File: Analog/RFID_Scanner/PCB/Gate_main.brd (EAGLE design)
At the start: 160 x 100 mm, 14 parts

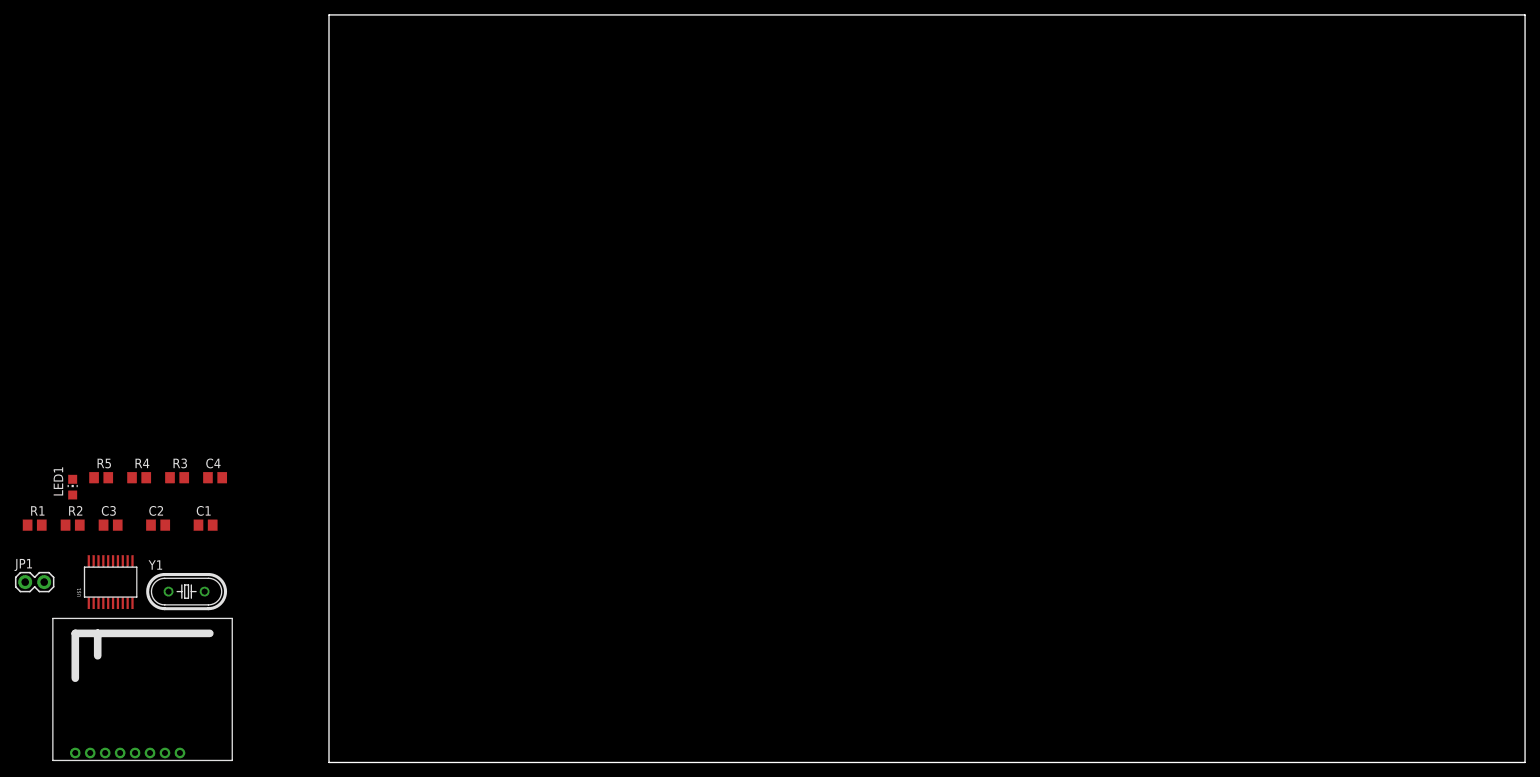
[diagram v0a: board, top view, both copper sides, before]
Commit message: PCB and firmware
Gate PCB 70% completed, need to figure out pinout for MCU and layout
signal amps.  Board size reduced by 50%.  Also need to add testpoints
Robot PCB PSU layout completed, motor and stepper drivers will move to
separate PCB
Created firmware files, w/o code
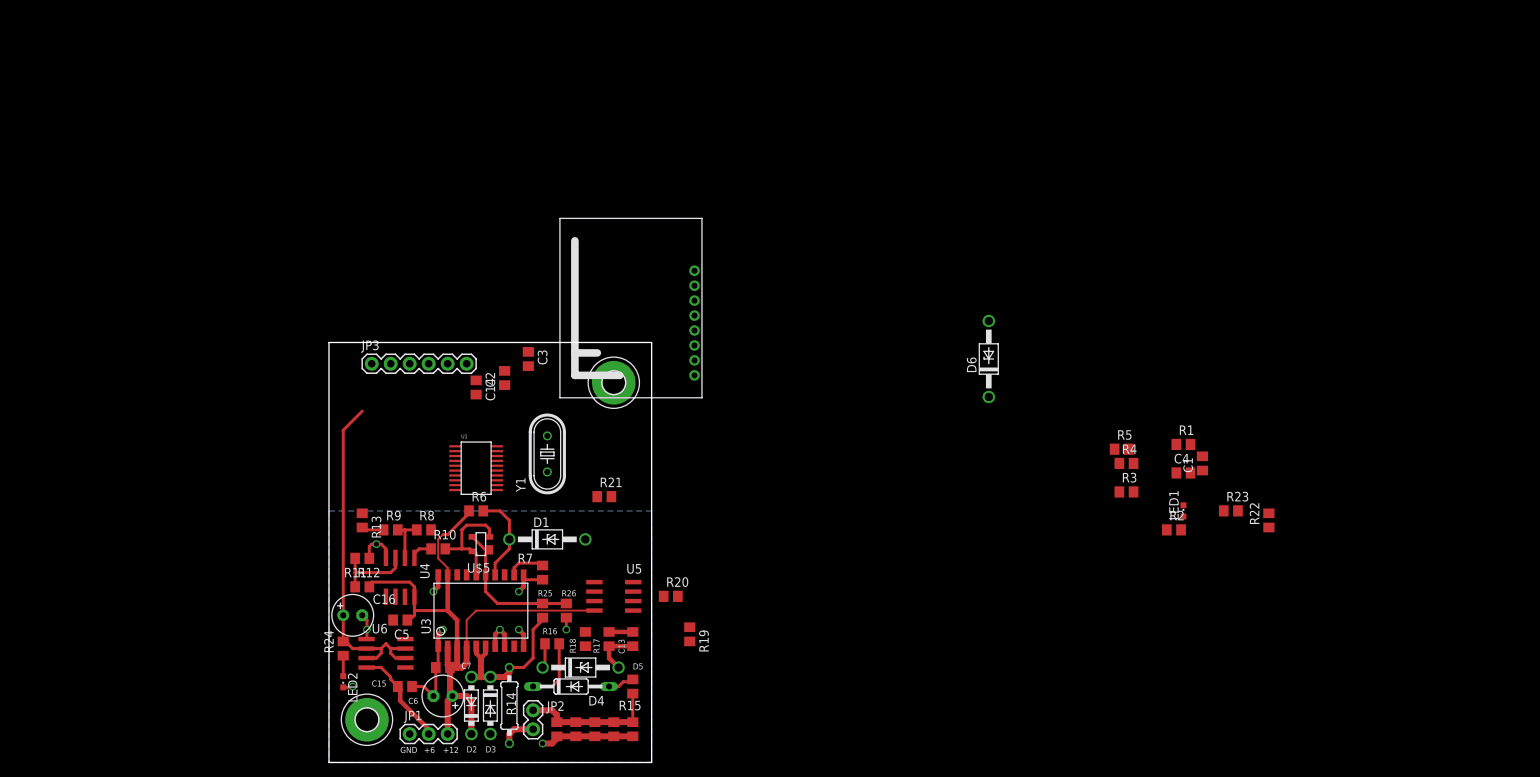
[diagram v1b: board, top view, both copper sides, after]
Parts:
- removed U$1: MSP430G2X53_20P, npol:TSSOP20_PW
- removed U$2: QFM-TRX-24G, npol:QFM-TRX1-24G
- added C10, C11, C12, C13, C8, C9: (no value), rcl:C0805
- added C14, C7: 0.1uF, rcl:C0805
- added C15, C5: 10nF, rcl:C0805
- added C16, C6: 47uF, rcl:E2,5-6
- added D1: 1N4732A, diode:DO41Z10
- added D2, D3: 1N5819-B, diode:DO41-7.6
- added D4: 1N4148DO35-10, diode:DO35-10
- added D5: 1N4742A, diode:DO41Z10
- added D6: 1N4728, diode:DO41Z10
- added H1, H2: MOUNT-PAD-ROUND3.0, holes:3,0-PAD
- added JP2: M02PTH, SparkFun-Connectors:1X02
- added JP3: (no value), SparkFun-Connectors:1X06
- added LED2: (no value), led:CHIPLED_0603
- added R10, R13, R15, R18, R23, R25: 0, rcl:R0805
- added R11, R12, R19, R20, R21, R22, R6, R8, R9: 10k, rcl:R0805
- added R14: (no value), rcl:0207/10
- added R16, R17: 68k, rcl:R0805
- added R24: 470, rcl:R0805
- added R26: DNP, rcl:R0805
- added R7: 7.5k, rcl:R0805
- added U$5: SMS3922-015LF, npol:SMS3922-015LF
- added U1: MSP430G2X53_20P, npol:TSSOP20_PW
- added U2: QFM-TRX-24G, npol:QFM-TRX1-24G
- added U3: OPA564, npol:SO-20LD
- added U4: OPA2134SO-8, npol:SOIC8
- added U5: LM6482, npol:SOIC8
- added U6: LD1117D33CTR, npol:SOIC8
- JP1: value M02PTH -> (none); device SparkFun-Connectors:1X02 -> SparkFun-Connectors:1X03
- LED1: device led:CHIP-LED0805 -> led:CHIPLED_0603
- moved R1 154.0 mm to (114.3, 42.5)
- moved LED1 148.6 mm to (114.3, 33.7)
- moved R2 147.3 mm to (113.0, 31.1)
- moved R5 136.6 mm to (106.0, 41.9)
- moved C1 133.6 mm to (116.8, 40.0), turned to 90 degrees
- moved R4 132.1 mm to (106.7, 40.0)
- moved C4 129.5 mm to (114.3, 38.7)
- moved R3 127.0 mm to (106.7, 36.2)
- moved C3 60.1 mm to (26.7, 54.0), turned to 270 degrees
- moved JP1 55.3 mm to (10.8, 3.81)
- moved Y1 51.7 mm to (29.2, 41.3), turned to 90 degrees
- moved C2 50.4 mm to (23.5, 51.4), turned to 90 degrees
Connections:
- new net +12V: C14.1, C5.1, C6.+, C7.1, D2.C, JP1.3, R12.2, R6.1, U3.19, U3.2, U3.3, U3.4, U4.8, U5.8
- new net +6V: C15.1, JP1.2, U6.4
- new net BIAS_OUT: R10.1, R8.2, U4.1
- new net ISET: R7.2, U3.12
- new net LC_SEN: C10.1, C11.1, C12.1, C8.1, C9.1, JP2.2, R15.2
- new net N$10: D4.C, R16.2
- new net N$11: D4.A, R15.1
- new net N$12: R25.1, R26.2, U$5.1, U$5.3, U3.15
- new net N$13: C13.1, D5.C, R16.1, R17.2, R18.2
- new net N$14: R18.1, R19.2
- new net N$15: R19.1, R20.2, U5.2
- new net N$16: R20.1, R21.2, U5.1
- new net N$17: R21.1, R22.2, R23.2
- new net N$19: LED2.A, R24.1
- new net N$5: R8.1, R9.2, U4.2
- new net N$6: R10.2, U$5.2, U$5.4, U3.16
- new net N$7: R11.2, R12.1, U4.3
- new net N$8: R13.2, R9.1
- new net N$9: JP2.1, R14.2
- new net PA_OUT: D2.A, D3.C, R14.1, R25.2, U3.5, U3.6
- new net RFID_RX: D6.C, R23.1, U1.9
- new net RFID_TX: R13.1, U1.8
- new net VDIG: D1.C, R6.2, U3.14
- new net VPROG: JP3.6
- net +3V3: now also C16.+, R24.2, U1.1, U2.1, U6.2, U6.3, U6.6, U6.7; no longer U$1.1, U$2.1
- net DLED: now also U1.2; no longer U$1.2
- net GND: now also C10.2, C11.2, C12.2, C13.2, C14.2, C15.2, C16.-, C5.2, C6.-, C7.2, C8.2, C9.2, D1.A, D3.A, D5.A, D6.A, H1.B3,0, H2.B3,0, JP1.1, JP3.1, LED2.C, R11.1, R17.1, R22.1, R26.1, R7.1, U1.20, U2.6, U3.1, U3.10, U3.11, U3.20, U3.7, U3.8, U4.4, U5.3, U5.4, U6.1; no longer U$1.20, U$2.6
- net MISO: now also U1.14; no longer U$1.14
- net MOSI: now also U1.15; no longer U$1.15
- net N$2: now also U2.4; no longer U$2.4
- net N$3: now also U2.3; no longer U$2.3
- net N$4: now also U2.2; no longer U$2.2
- net RXD: now also JP3.3, U1.3; no longer U$1.3
- net SBWTCK: now also JP3.5, U1.17; no longer U$1.17
- net SBWTDIO: now also JP3.4, U1.16; no longer U$1.16
- net SCK: now also U1.7; no longer U$1.7
- net TXD: now also JP3.2, U1.4; no longer U$1.4
- net XIN: now also U1.19; no longer U$1.19
- net XOUT: now also U1.18; no longer U$1.18
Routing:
- net +12V: track 0.00 -> 85.6 mm
- net GND: track 0.00 -> 58.9 mm, vias 0 -> 10
- net +3V3: track 0.00 -> 46.8 mm
- net PA_OUT: track 0.00 -> 21.8 mm
- net N$12: track 0.00 -> 20.3 mm
- net LC_SEN: track 0.00 -> 18.4 mm
- net N$6: track 0.00 -> 15.0 mm
- net +6V: track 0.00 -> 13.5 mm
- net VDIG: track 0.00 -> 12.1 mm
- net N$7: track 0.00 -> 10.8 mm
- net N$10: track 0.00 -> 8.65 mm
- net N$13: track 0.00 -> 6.48 mm
- net N$5: track 0.00 -> 6.29 mm
- net ISET: track 0.00 -> 5.15 mm
- net N$9: track 0.00 -> 4.71 mm
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- added copper zone on layer 16, net GND
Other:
- board size 160 x 100 mm -> 43.2 x 56.2 mm
- board text added: "+12"
- board text added: "+6"
- board text added: "GND"

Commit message: Gate PCB progress
Did layout for gate pcb signal amps, finalized board size, added
testpoints
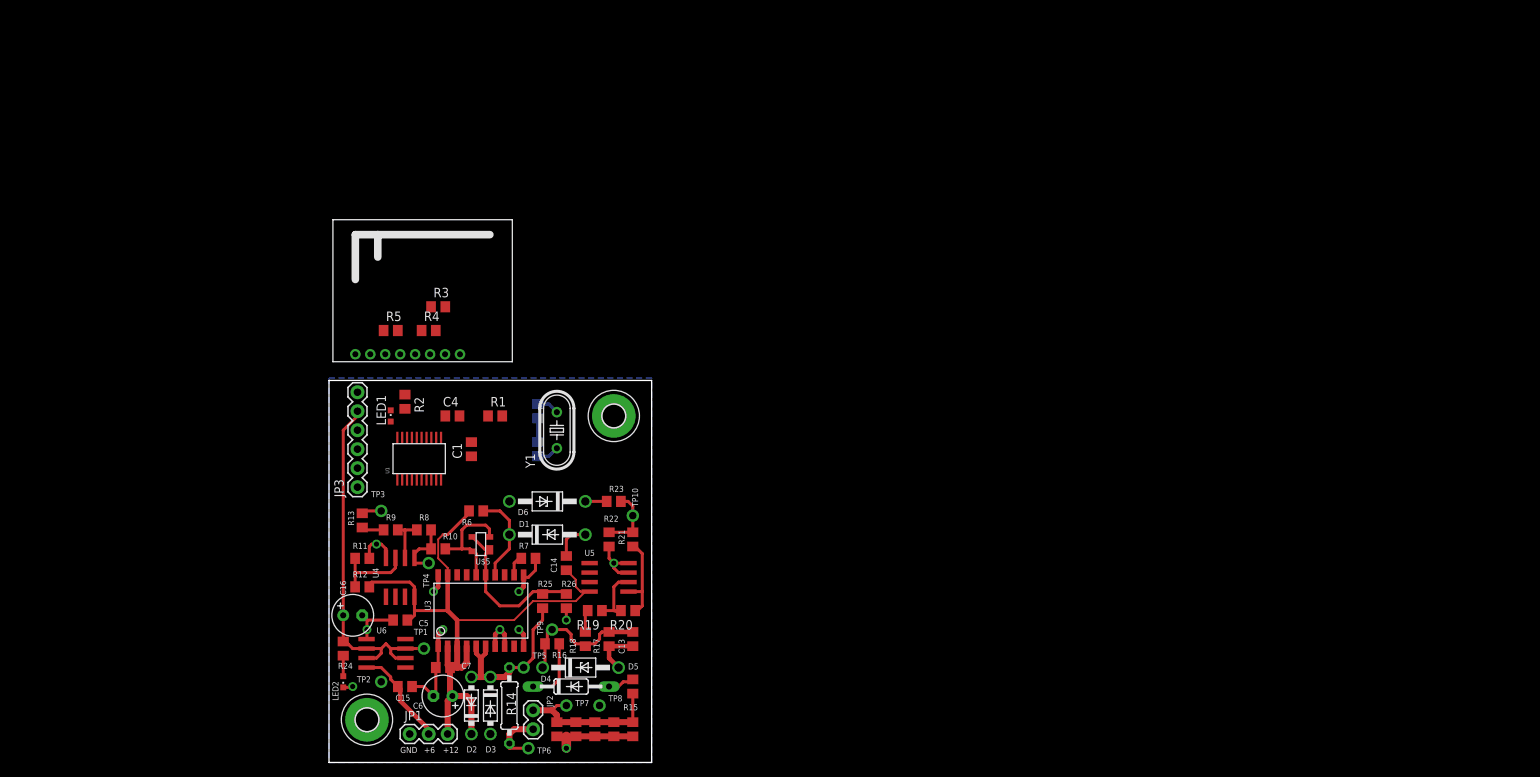
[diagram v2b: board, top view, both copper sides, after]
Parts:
- added TP1, TP10, TP2, TP3, TP4, TP5, TP6, TP7, TP8, TP9: (no value), microbuilder:1X01_ROUND
- C15: value 10nF -> 100nF
- moved LED1 106.8 mm to (8.26, 46.4)
- moved R2 104.3 mm to (10.2, 48.3), turned to 270 degrees
- moved R5 99.1 mm to (8.26, 57.8)
- moved C4 98.1 mm to (16.5, 46.4)
- moved C1 97.8 mm to (19.1, 41.9)
- moved R3 95.3 mm to (14.6, 61.0)
- moved R4 95.0 mm to (13.3, 57.8)
- moved R1 92.2 mm to (22.2, 46.4)
- moved R22 88.3 mm to (37.5, 29.8)
- moved R23 82.6 mm to (38.1, 34.9)
- moved D6 62.1 mm to (29.2, 34.9), turned to 180 degrees
- moved U2 39.5 mm to (9.53, 54.6), turned to 0 degrees
- moved C14 26.4 mm to (31.8, 26.7), turned to 90 degrees
- moved JP3 16.6 mm to (3.81, 36.8), turned to 90 degrees
- moved R19 13.1 mm to (35.6, 20.3), turned to 180 degrees
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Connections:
- removed net DLED: LED1.C, U1.2
- new net N$18: R2.2, U1.2
- net +3V3: now also TP1.1; no longer R2.2
- net BIAS_OUT: now also TP4.1
- net GND: now also LED1.C, TP2.1
- net LC_SEN: now also TP7.1
- net N$10: now also TP8.1
- net N$13: now also TP9.1
- net N$17: now also TP10.1
- net N$9: now also TP6.1
- net PA_OUT: now also TP5.1
- net RFID_TX: now also TP3.1
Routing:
- net GND: track 58.9 -> 78.0 mm, vias 10 -> 11
- net N$13: track 6.48 -> 19.2 mm
- net N$16: track 0.00 -> 11.7 mm
- net N$15: track 0.00 -> 9.28 mm
- net N$17: track 0.00 -> 8.52 mm
- net BIAS_OUT: track 3.06 -> 8.21 mm
- net N$9: track 4.71 -> 7.88 mm
- net N$14: track 0.00 -> 2.99 mm
- net XOUT: track 0.00 -> 2.99 mm
- net XIN: track 0.00 -> 2.99 mm
- net RFID_TX: track 0.00 -> 2.86 mm
- net RFID_RX: track 0.00 -> 2.86 mm
- net +3V3: track 46.8 -> 49.3 mm
- net +12V: track 85.6 -> 88.1 mm
- net ISET: track 5.15 -> 2.79 mm
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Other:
- board size 43.2 x 56.2 mm -> 43.2 x 51.1 mm

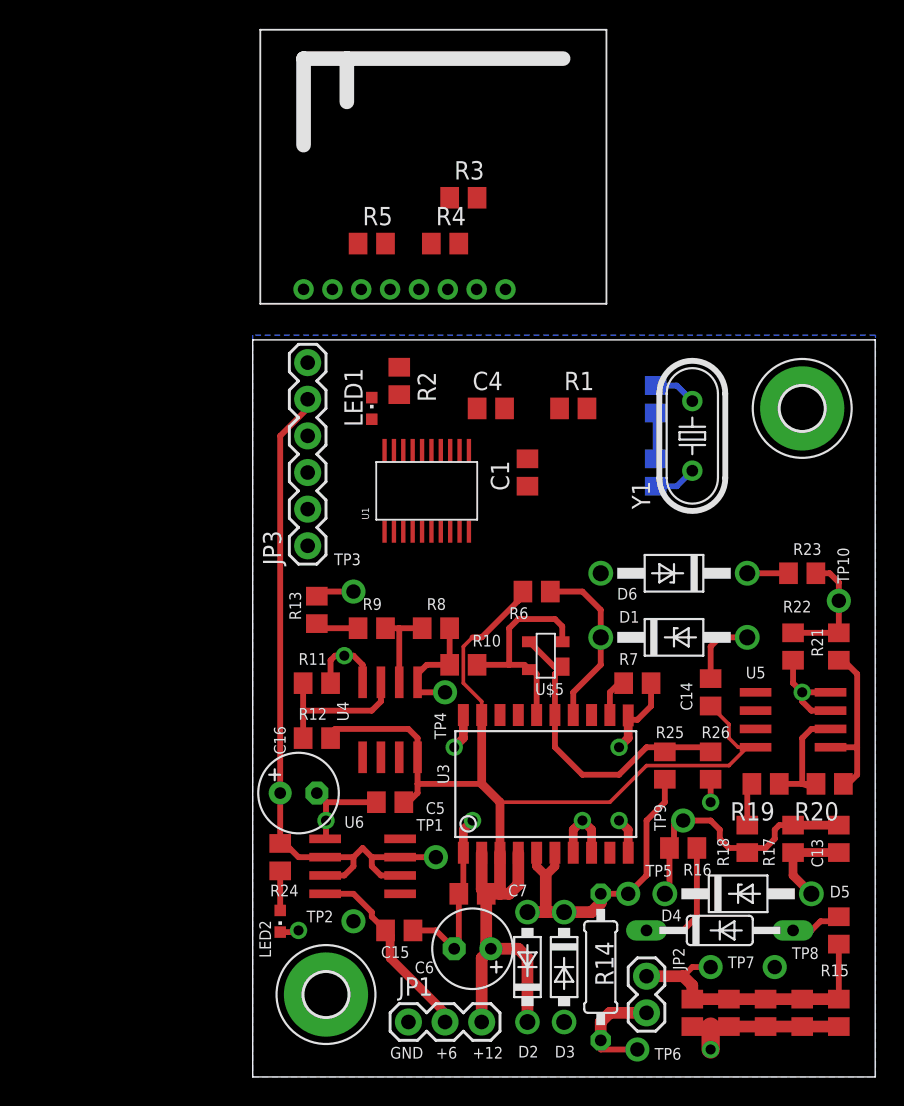
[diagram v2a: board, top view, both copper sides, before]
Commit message: Board final; SPI progress
Sent PCBs to FAB
SPI driver working for multi-byte.  Bug: bytes are sent in reversed
order, although bit ordering (MSB first) is correct.
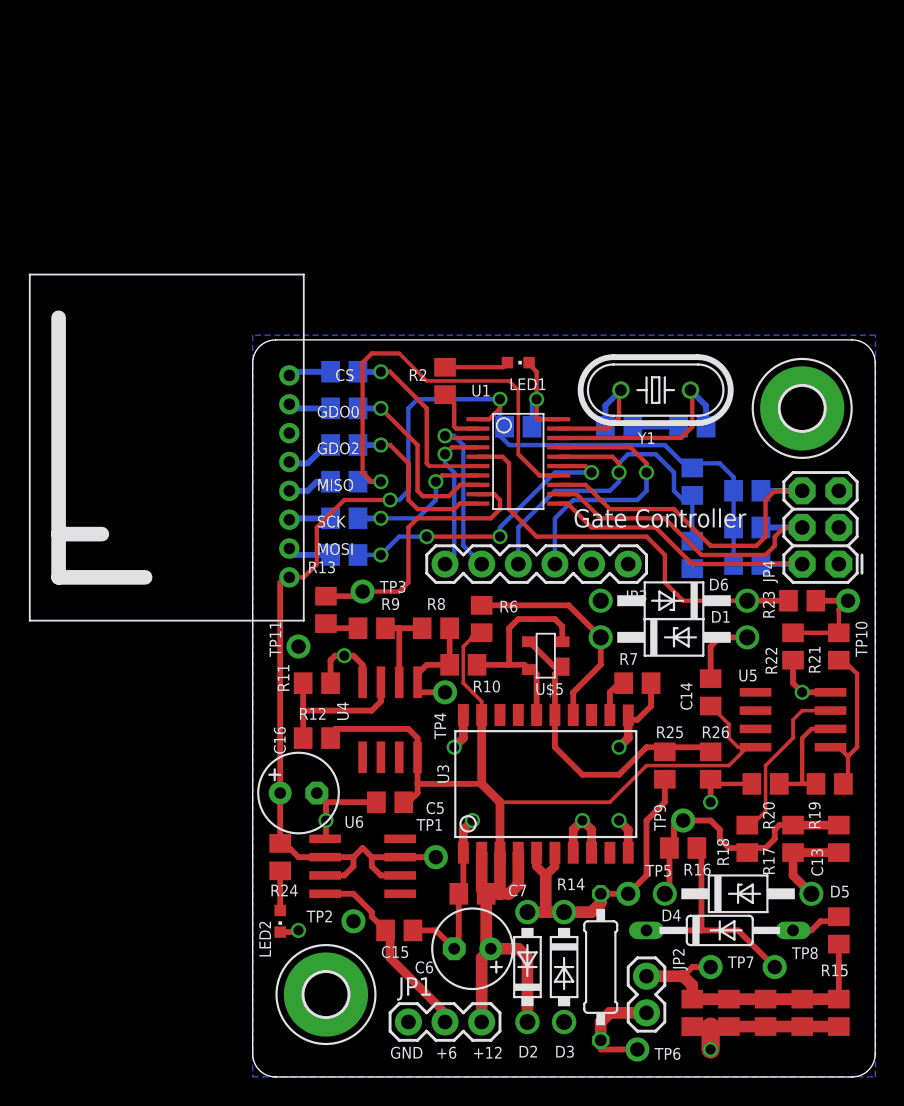
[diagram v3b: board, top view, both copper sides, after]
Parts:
- added JP4: (no value), SparkFun-Connectors:2X3
- added R27, R28, R29: 0, rcl:R0805
- added R30, R31, R32: 10k, rcl:R0805
- added TP11: (no value), microbuilder:1X01_ROUND
- C13: value (none) -> 6.8n
- R11: value 10k -> 12k
- R12, R21: value 10k -> 33k
- R19: value 10k -> 0
- R20: value 10k -> DNP
- R8: value 10k -> 15k
- R9: value 10k -> 8.2k
- U1: value MSP430G2X53_20P -> MSP430G2X53_20PPW; device npol:TSSOP20_PW -> npol:PW(R-PDSO-G20)
- Y1: value (none) -> 8MHz
- moved R3 26.1 mm to (6.35, 36.2), flipped to the bottom, turned to 180 degrees
- moved JP3 22.3 mm to (26.0, 35.6), turned to 180 degrees
- moved R4 20.3 mm to (6.35, 38.7), flipped to the bottom, turned to 180 degrees
- moved C4 17.3 mm to (30.5, 36.2), flipped to the bottom, turned to 270 degrees
- moved R5 16.6 mm to (6.35, 41.3), flipped to the bottom, turned to 180 degrees
- moved U2 15.6 mm to (2.54, 40.6), turned to 90 degrees
- moved LED1 10.6 mm to (18.4, 49.5), turned to 270 degrees
- moved R1 9.69 mm to (30.5, 41.3), flipped to the bottom, turned to 90 degrees
- moved U1 6.84 mm to (18.4, 43.2), turned to 270 degrees
- moved R19 4.45 mm to (40.0, 20.3), turned to 0 degrees
- moved R20 4.45 mm to (35.6, 20.3), turned to 0 degrees
- moved R6 4.26 mm to (15.9, 31.8), turned to 90 degrees
- moved C2 4.07 mm to (30.5, 45.1), turned to 0 degrees
- moved Y1 4.07 mm to (27.9, 47.6), turned to 180 degrees
- moved C1 3.24 mm to (18.4, 45.1), flipped to the bottom, turned to 180 degrees
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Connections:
- removed net N$14 (its old number): R18.1, R19.2
- new net CS: R29.2, U1.6
- new net GDO0: R28.2, U1.8
- new net GDO2: R27.2, U1.10
- new net ID0: JP4.2, R30.1, U1.11
- new net ID1: JP4.4, R31.1, U1.12
- new net ID2: JP4.6, R32.1, U1.13
- new net N$15: R19.2, R21.1, U5.1
- new net N$20: R29.1, U2.8
- new net N$21: R28.1, U2.7
- new net N$22: R27.1, U2.5
- net +3V3: now also R30.2, R31.2, R32.2
- net GND: now also JP4.1, JP4.3, JP4.5, R20.1; no longer U5.3
- net N$16: now also R18.1, U5.3; no longer R20.1, R21.2, U5.1
- net N$17: now also R21.2; no longer R21.1
- net N$8: now also TP11.1
- net RFID_RX: now also U1.5; no longer U1.9
- net RFID_TX: now also U1.9; no longer U1.8
- net RXD: now also JP3.5; no longer JP3.3
- net SBWTCK: now also JP3.3; no longer JP3.5
- net TXD: now also JP3.6; no longer JP3.2
- net VPROG: now also JP3.2; no longer JP3.6
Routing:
- net +3V3: track 49.3 -> 90.0 mm, vias 0 -> 2
- net MISO: track 0.00 -> 30.7 mm, vias 0 -> 1
- net SBWTDIO: track 0.00 -> 27.8 mm, vias 0 -> 1
- net RFID_RX: track 2.86 -> 28.6 mm
- net ID2: track 0.00 -> 24.6 mm
- net ID1: track 0.00 -> 22.6 mm
- net ID0: track 0.00 -> 21.5 mm
- net MOSI: track 0.00 -> 21.4 mm, vias 0 -> 4
- net SBWTCK: track 0.00 -> 18.8 mm, vias 0 -> 1
- net RFID_TX: track 2.86 -> 19.1 mm
- net CS: track 0.00 -> 13.3 mm, vias 0 -> 1
- net GDO0: track 0.00 -> 13.0 mm, vias 0 -> 1
- net RXD: track 0.00 -> 12.7 mm, vias 0 -> 1
- net XOUT: track 2.99 -> 15.2 mm
- net GDO2: track 0.00 -> 11.8 mm, vias 0 -> 1
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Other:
- outline, holes or cut-outs redrawn
- board text added: "2014 Nishant Pol"
- board text added: "Build18 2015"
- board text added: "CS"
- board text added: "GDO0"
- board text added: "GDO2"
- board text added: "Gate Controller"
- board text added: "MISO"
- board text added: "MOSI"
- board text added: "RFID Localization"
- board text added: "SCK"
